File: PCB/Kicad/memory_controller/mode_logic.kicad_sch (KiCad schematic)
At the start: 4 parts, among them U23 6xNOT__SN74HC14DR, U24 4xAND__SN74HC08DR

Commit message: fix
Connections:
- net nOE_n renamed ~{OE}_n
- net nOE_p renamed ~{OE}_p
- net nOUTPUT_ENABLE renamed ~{OUTPUT_ENABLE}
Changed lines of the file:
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@@
 		)
 	)
-	(hierarchical_label "nOE_p"
+	(hierarchical_label "~{OE}_p"
 		(shape output)
 		(at 152.4 66.04 0)
@@
 		)
 	)
-	(hierarchical_label "nOE_n"
+	(hierarchical_label "~{OE}_n"
 		(shape output)
 		(at 152.4 38.1 0)
@@
 		)
 	)
-	(hierarchical_label "nOUTPUT_ENABLE"
+	(hierarchical_label "~{OUTPUT_ENABLE}"
 		(shape output)
 		(at 152.4 63.5 0)

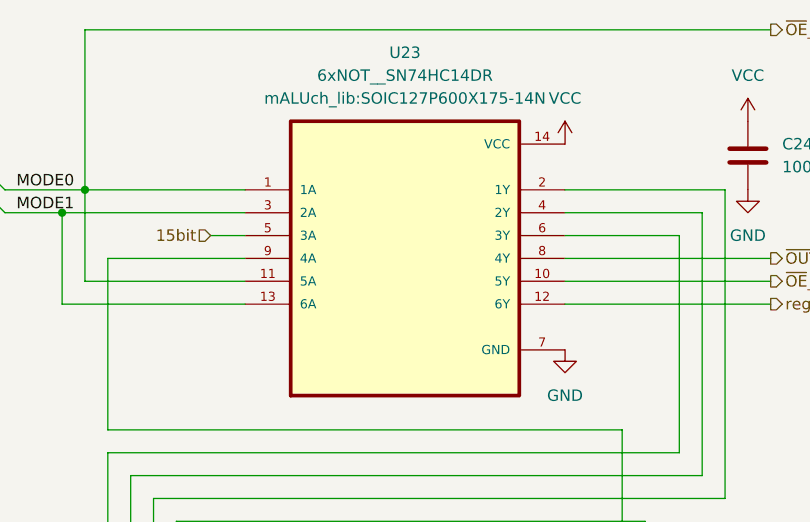
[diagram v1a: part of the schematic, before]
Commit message: memory controler fix
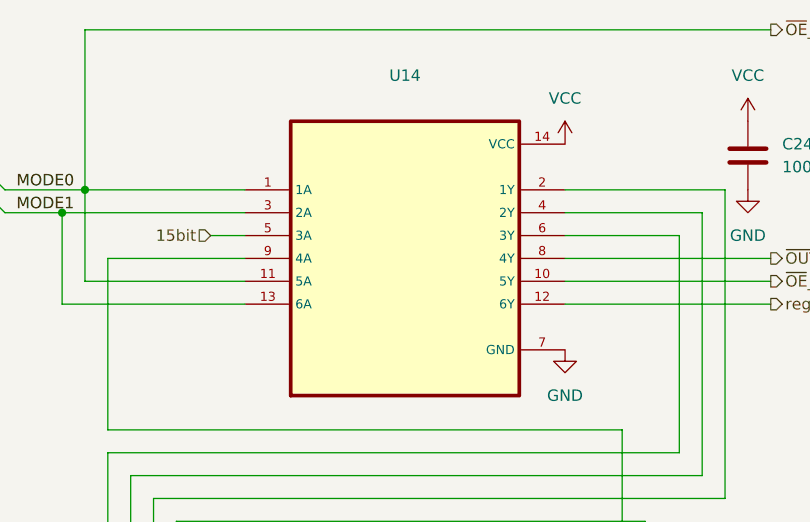
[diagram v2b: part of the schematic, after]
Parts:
- removed U23: 6xNOT__SN74HC14DR, mALUch_lib:SOIC127P600X175-14N, symbol mALUch_lib:6xNOT__SN74HC14DR
- added U14: ~, mALUch_lib:SOIC127P600X175-14N, symbol mALUch_lib:6xNOT__SN74HC04DR
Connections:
- net 15bit: now also U14.5 (3A)
- net GND: now also U14.7 (GND)
- net MODE1: now also U14.13 (6A), U14.3 (2A)
- net OUTPUT_ENABLE: now also U14.9 (4A)
- net VCC: now also U14.14 (VCC)
- net reg_clk_en: now also U14.12 (6Y)
- net ~{OE}_n: now also U14.1 (1A), U14.11 (5A)
- net ~{OE}_p: now also U14.10 (5Y)
- net ~{OUTPUT_ENABLE}: now also U14.8 (4Y)
- net at U24.12 (4A): now also U14.4 (2Y)
- net at U24.13 (4B): now also U14.2 (1Y)
- net at U24.5 (2B): now also U14.6 (3Y)

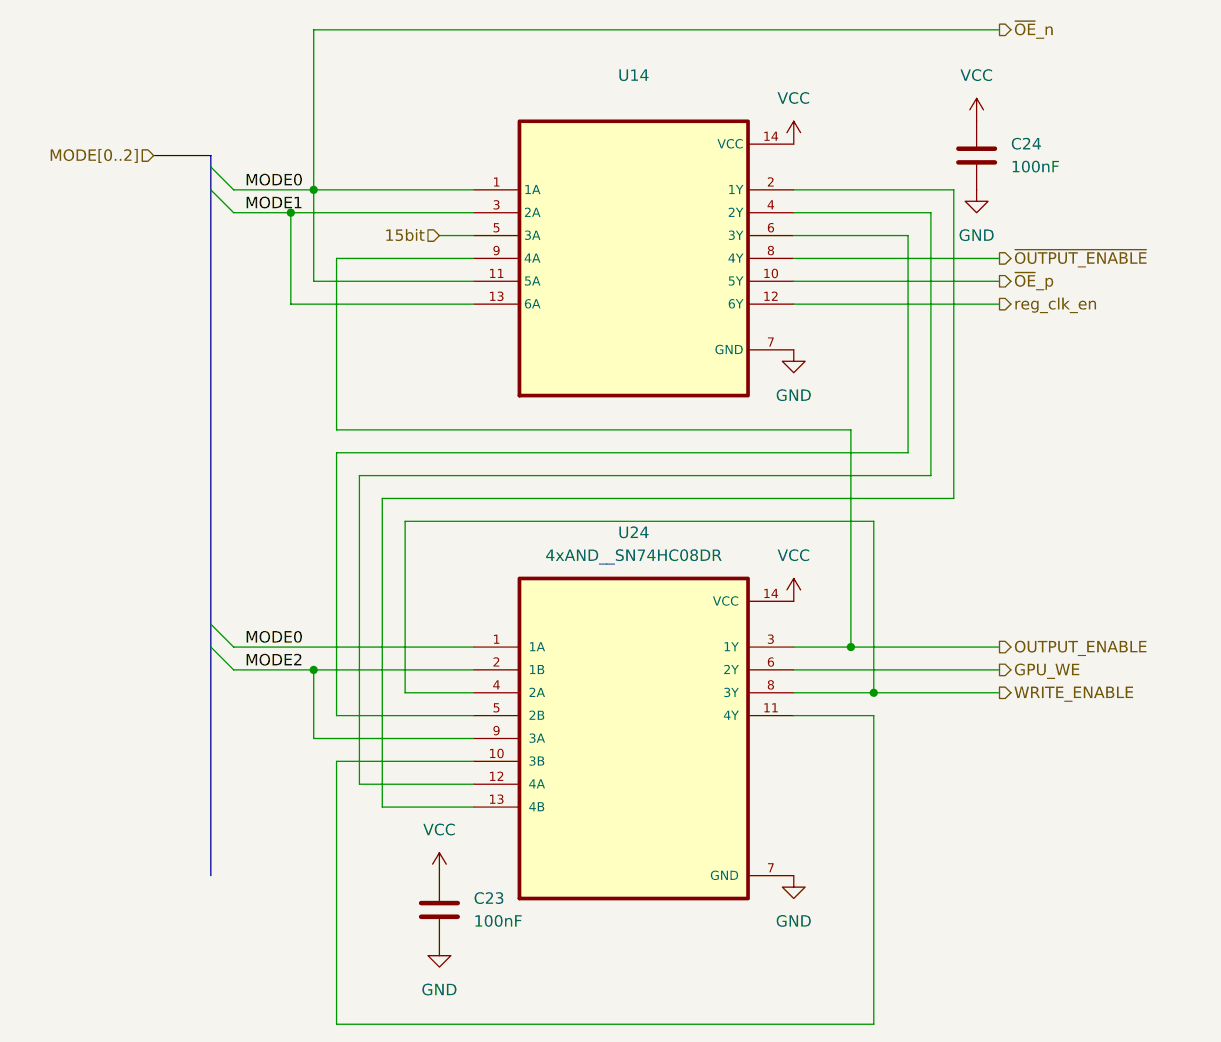
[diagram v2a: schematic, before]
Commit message: kicad fix
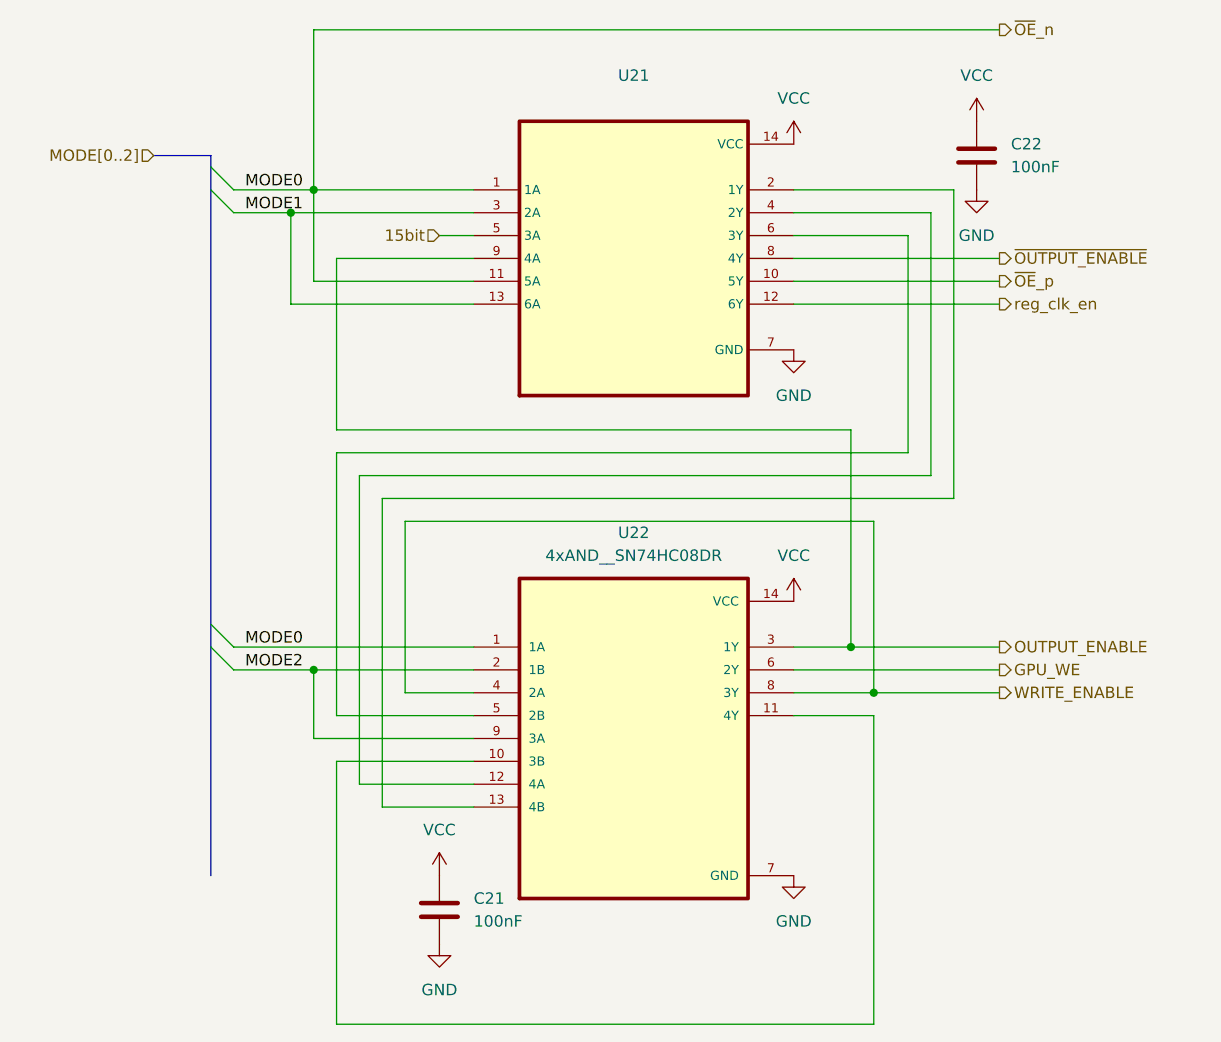
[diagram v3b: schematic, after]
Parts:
- renumbered C23 to C21, C24 to C22, U14 to U21, U24 to U22
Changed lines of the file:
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@@
 		(dnp no)
 		(fields_autoplaced yes)
-		(property "Reference" "C24"
+		(property "Reference" "C22"
 			(at 153.67 50.7999 0)
 			(effects
@@
 			(project "memory_controller"
 				(path "/dccec861-b967-466c-843e-d6d1ad6064ce/567eb6ac-0bde-47ed-8069-dee677659fff"
-					(reference "C24")
+					(reference "C22")
 					(unit 1)
 				)
@@
 		(dnp no)
 		(fields_autoplaced yes)
-		(property "Reference" "U24"
+		(property "Reference" "U22"
 			(at 111.76 93.98 0)
 			(effects
@@
 			(project ""
 				(path "/dccec861-b967-466c-843e-d6d1ad6064ce/567eb6ac-0bde-47ed-8069-dee677659fff"
-					(reference "U24")
+					(reference "U22")
 					(unit 1)
 				)
@@
 		(dnp no)
 		(fields_autoplaced yes)
-		(property "Reference" "#PWR0121"
+		(property "Reference" "#PWR0111"
 			(at 149.86 52.07 0)
 			(effects
@@
 			(project "memory_controller"
 				(path "/dccec861-b967-466c-843e-d6d1ad6064ce/567eb6ac-0bde-47ed-8069-dee677659fff"
-					(reference "#PWR0121")
+					(reference "#PWR0111")
 					(unit 1)
 				)
@@
 		(dnp no)
 		(fields_autoplaced yes)
-		(property "Reference" "#PWR0115"
+		(property "Reference" "#PWR0105"
 			(at 90.17 135.89 0)
 			(effects
@@
 			(project "memory_controller"
 				(path "/dccec861-b967-466c-843e-d6d1ad6064ce/567eb6ac-0bde-47ed-8069-dee677659fff"
-					(reference "#PWR0115")
+					(reference "#PWR0105")
 					(unit 1)
 				)
@@
 		(dnp no)
 		(fields_autoplaced yes)
-		(property "Reference" "#PWR0118"
+		(property "Reference" "#PWR0108"
 			(at 129.54 80.01 0)
 			(effects
@@
 			(project "memory_controller"
 				(path "/dccec861-b967-466c-843e-d6d1ad6064ce/567eb6ac-0bde-47ed-8069-dee677659fff"
-					(reference "#PWR0118")
+					(reference "#PWR0108")
 					(unit 1)
 				)
@@
 		(dnp no)
 		(fields_autoplaced yes)
-		(property "Reference" "#PWR0120"
+		(property "Reference" "#PWR0110"
 			(at 129.54 138.43 0)
 			(effects
@@
 			(project ""
 				(path "/dccec861-b967-466c-843e-d6d1ad6064ce/567eb6ac-0bde-47ed-8069-dee677659fff"
-					(reference "#PWR0120")
+					(reference "#PWR0110")
 					(unit 1)
 				)
@@
 		(dnp no)
 		(fields_autoplaced yes)
-		(property "Reference" "C23"
+		(property "Reference" "C21"
 			(at 93.98 134.6199 0)
 			(effects
@@
 			(project ""
 				(path "/dccec861-b967-466c-843e-d6d1ad6064ce/567eb6ac-0bde-47ed-8069-dee677659fff"
-					(reference "C23")
+					(reference "C21")
 					(unit 1)
 				)
@@
 		(dnp no)
 		(fields_autoplaced yes)
-		(property "Reference" "#PWR0122"
+		(property "Reference" "#PWR0112"
 			(at 149.86 62.23 0)
 			(effects
@@
 			(project "memory_controller"
 				(path "/dccec861-b967-466c-843e-d6d1ad6064ce/567eb6ac-0bde-47ed-8069-dee677659fff"
-					(reference "#PWR0122")
+					(reference "#PWR0112")
 					(unit 1)
 				)
@@
 		(dnp no)
 		(fields_autoplaced yes)
-		(property "Reference" "#PWR0117"
+		(property "Reference" "#PWR0107"
 			(at 129.54 54.61 0)
 			(effects
@@
 			(project "memory_controller"
 				(path "/dccec861-b967-466c-843e-d6d1ad6064ce/567eb6ac-0bde-47ed-8069-dee677659fff"
-					(reference "#PWR0117")
+					(reference "#PWR0107")
 					(unit 1)
 				)
@@
 		(dnp no)
 		(fields_autoplaced yes)
-		(property "Reference" "#PWR0116"
+		(property "Reference" "#PWR0106"
 			(at 90.17 146.05 0)
 			(effects
@@
 			(project "memory_controller"
 				(path "/dccec861-b967-466c-843e-d6d1ad6064ce/567eb6ac-0bde-47ed-8069-dee677659fff"
-					(reference "#PWR0116")
+					(reference "#PWR0106")
 					(unit 1)
 				)
@@
 		(dnp no)
 		(fields_autoplaced yes)
-		(property "Reference" "#PWR0119"
+		(property "Reference" "#PWR0109"
 			(at 129.54 105.41 0)
 			(effects
@@
 			(project ""
 				(path "/dccec861-b967-466c-843e-d6d1ad6064ce/567eb6ac-0bde-47ed-8069-dee677659fff"
-					(reference "#PWR0119")
+					(reference "#PWR0109")
 					(unit 1)
 				)
@@
 		(dnp no)
 		(fields_autoplaced yes)
-		(property "Reference" "U14"
+		(property "Reference" "U21"
 			(at 111.76 43.18 0)
 			(effects
@@
 			(project ""
 				(path "/dccec861-b967-466c-843e-d6d1ad6064ce/567eb6ac-0bde-47ed-8069-dee677659fff"
-					(reference "U14")
-					(unit 1)
-				)
+					(reference "U21")
+					(unit 1)
+				)

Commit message: pcb init
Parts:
- C21, C22: footprint (none) -> Capacitor_SMD:C_0402_1005Metric
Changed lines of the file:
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@@
 			)
 		)
-		(property "Footprint" ""
+		(property "Footprint" "Capacitor_SMD:C_0402_1005Metric"
 			(at 148.8948 48.26 0)
 			(effects
@@
 			)
 		)
-		(property "Footprint" ""
+		(property "Footprint" "Capacitor_SMD:C_0402_1005Metric"
 			(at 89.2048 132.08 0)
 			(effects

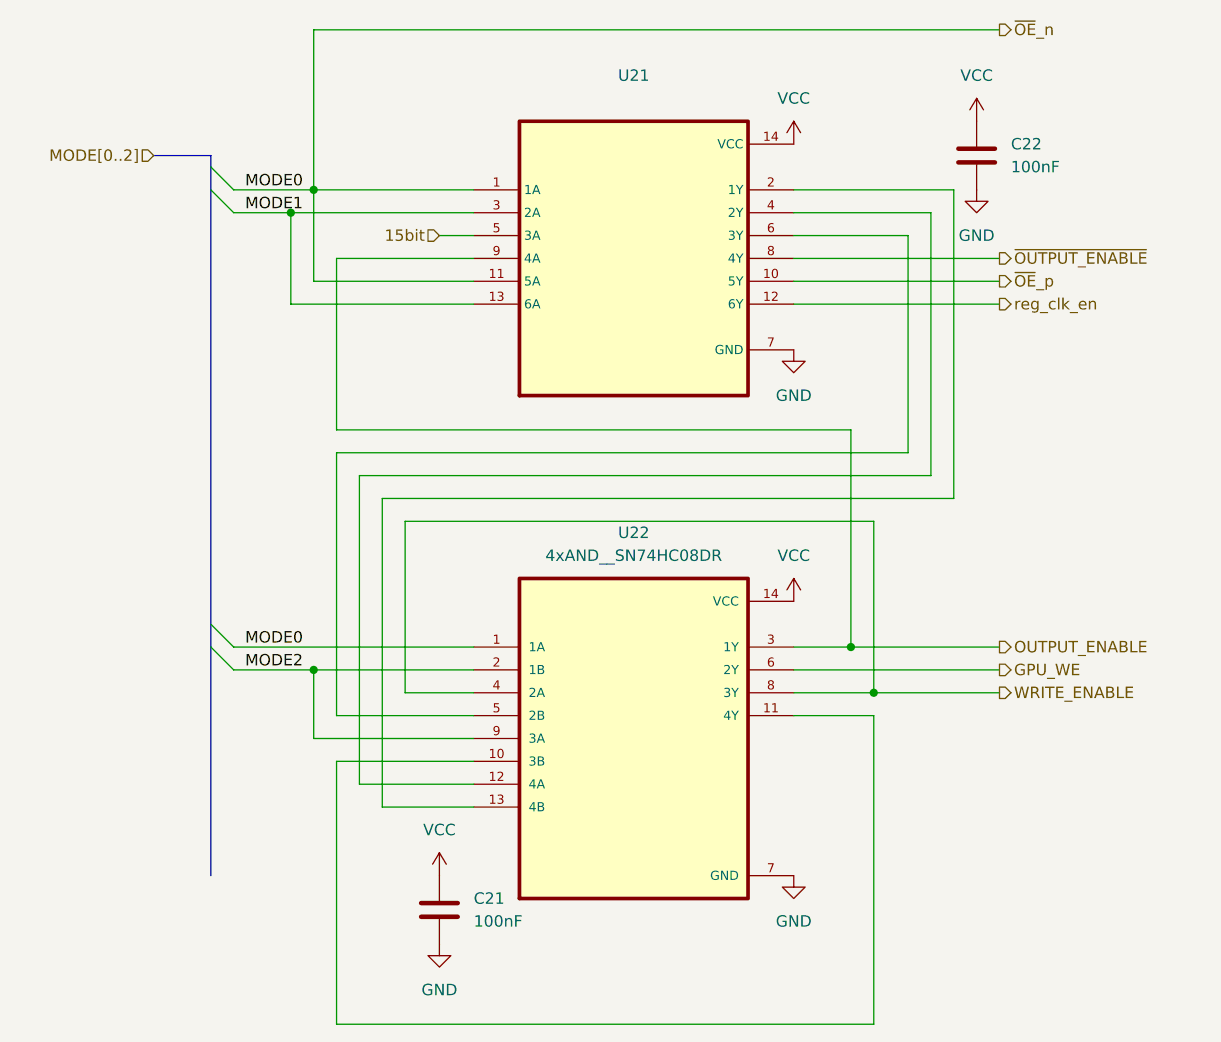
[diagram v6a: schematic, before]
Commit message: memory controller schematic update
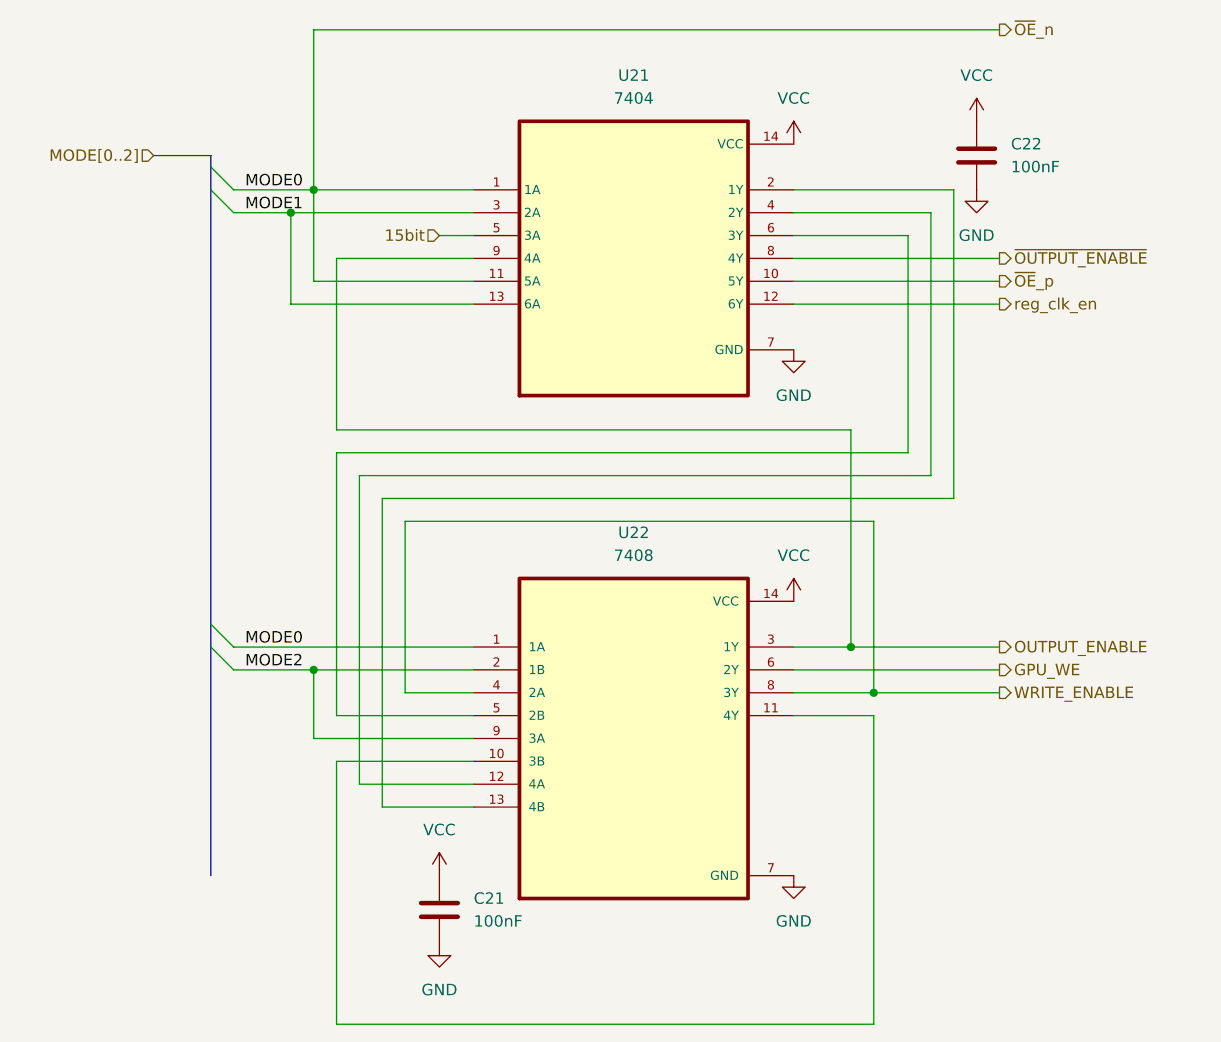
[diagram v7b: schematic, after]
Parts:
- U21: value ~ -> 7404; footprint mALUch_lib:SOIC127P600X175-14N -> Package_SO:SO-14_3.9x8.65mm_P1.27mm
- U22: value 4xAND__SN74HC08DR -> 7408; footprint mALUch_lib:SOIC127P600X175-14N -> Package_SO:SO-14_3.9x8.65mm_P1.27mm
